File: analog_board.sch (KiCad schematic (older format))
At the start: 48 parts, among them J301 SAMTEC-TSW-105-07-X-D, J302 SAMTEC-TSW-105-07-X-D, J304 SAMTEC-TSW-105-07-X-D, J305 SAMTEC-TSW-105-07-X-D, U1 LM324, U3 AD620, U4 AD620

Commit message: Most wiring is done, no ground yet
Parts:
- added R10, R21: 0R, Resistor_SMD:R_1206_3216Metric_Pad1.42x1.75mm_HandSolder, symbol Device:R
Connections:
- net Current_ch1_out: now also R21.1; no longer C12.1, R6.1
- net Current_sensor_1: now also R10.2; no longer R1.2, R2.2, R3.2, R5.2
- new net: R1.2, R10.1, R2.2, R3.2, R5.2
- new net: C12.1, R21.2, R6.1
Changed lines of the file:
@@
 	1    0    0    -1
 $EndComp
-Text Label 1450 4800 0    50   ~ 0
+Text Label 850  4800 0    50   ~ 0
 Current_sensor_1
 $Comp
@@
 	5250 6100 5250 6350
 Wire Wire Line
-	6300 4600 5700 4600
-Text Label 6300 4600 0    50   ~ 0
+	6900 4600 6300 4600
+Text Label 6900 4600 0    50   ~ 0
 Current_ch1_out
 Wire Wire Line
@@
 Wire Wire Line
 	2150 4750 2150 4800
-Connection ~ 2150 4800
 Wire Wire Line
 	2400 4750 2400 4800
@@
 Wire Wire Line
 	2400 4800 2150 4800
-Wire Wire Line
-	1400 4800 2150 4800
 $Comp
 L Amplifier_Instrumentation:AD620 U4
@@
 NoConn ~ 1550 13250
 NoConn ~ 1550 13350
-Connection ~ 5700 4600
 Wire Wire Line
 	17500 4600 16900 4600
@@
 Wire Wire Line
 	15850 4900 15850 5100
+$Comp
+L Device:R R10
+U 1 1 5C792D0B
+P 1850 4800
+F 0 "R10" V 1643 4800 50  0000 C CNN
+F 1 "0R" V 1734 4800 50  0000 C CNN
+F 2 "Resistor_SMD:R_1206_3216Metric_Pad1.42x1.75mm_HandSolder" V 1780 4800 50  0001 C CNN
+F 3 "~" H 1850 4800 50  0001 C CNN
+	1    1850 4800
+	0    1    1    0
+$EndComp
+Wire Wire Line
+	800  4800 1700 4800
+Wire Wire Line
+	2000 4800 2150 4800
+Connection ~ 2150 4800
+$Comp
+L Device:R R21
+U 1 1 5C7A1976
+P 6150 4600
+F 0 "R21" V 5943 4600 50  0000 C CNN
+F 1 "0R" V 6034 4600 50  0000 C CNN
+F 2 "Resistor_SMD:R_1206_3216Metric_Pad1.42x1.75mm_HandSolder" V 6080 4600 50  0001 C CNN
+F 3 "~" H 6150 4600 50  0001 C CNN
+	1    6150 4600
+	0    1    1    0
+$EndComp
+Wire Wire Line
+	5700 4600 6000 4600
+Connection ~ 5700 4600
 $EndSCHEMATC

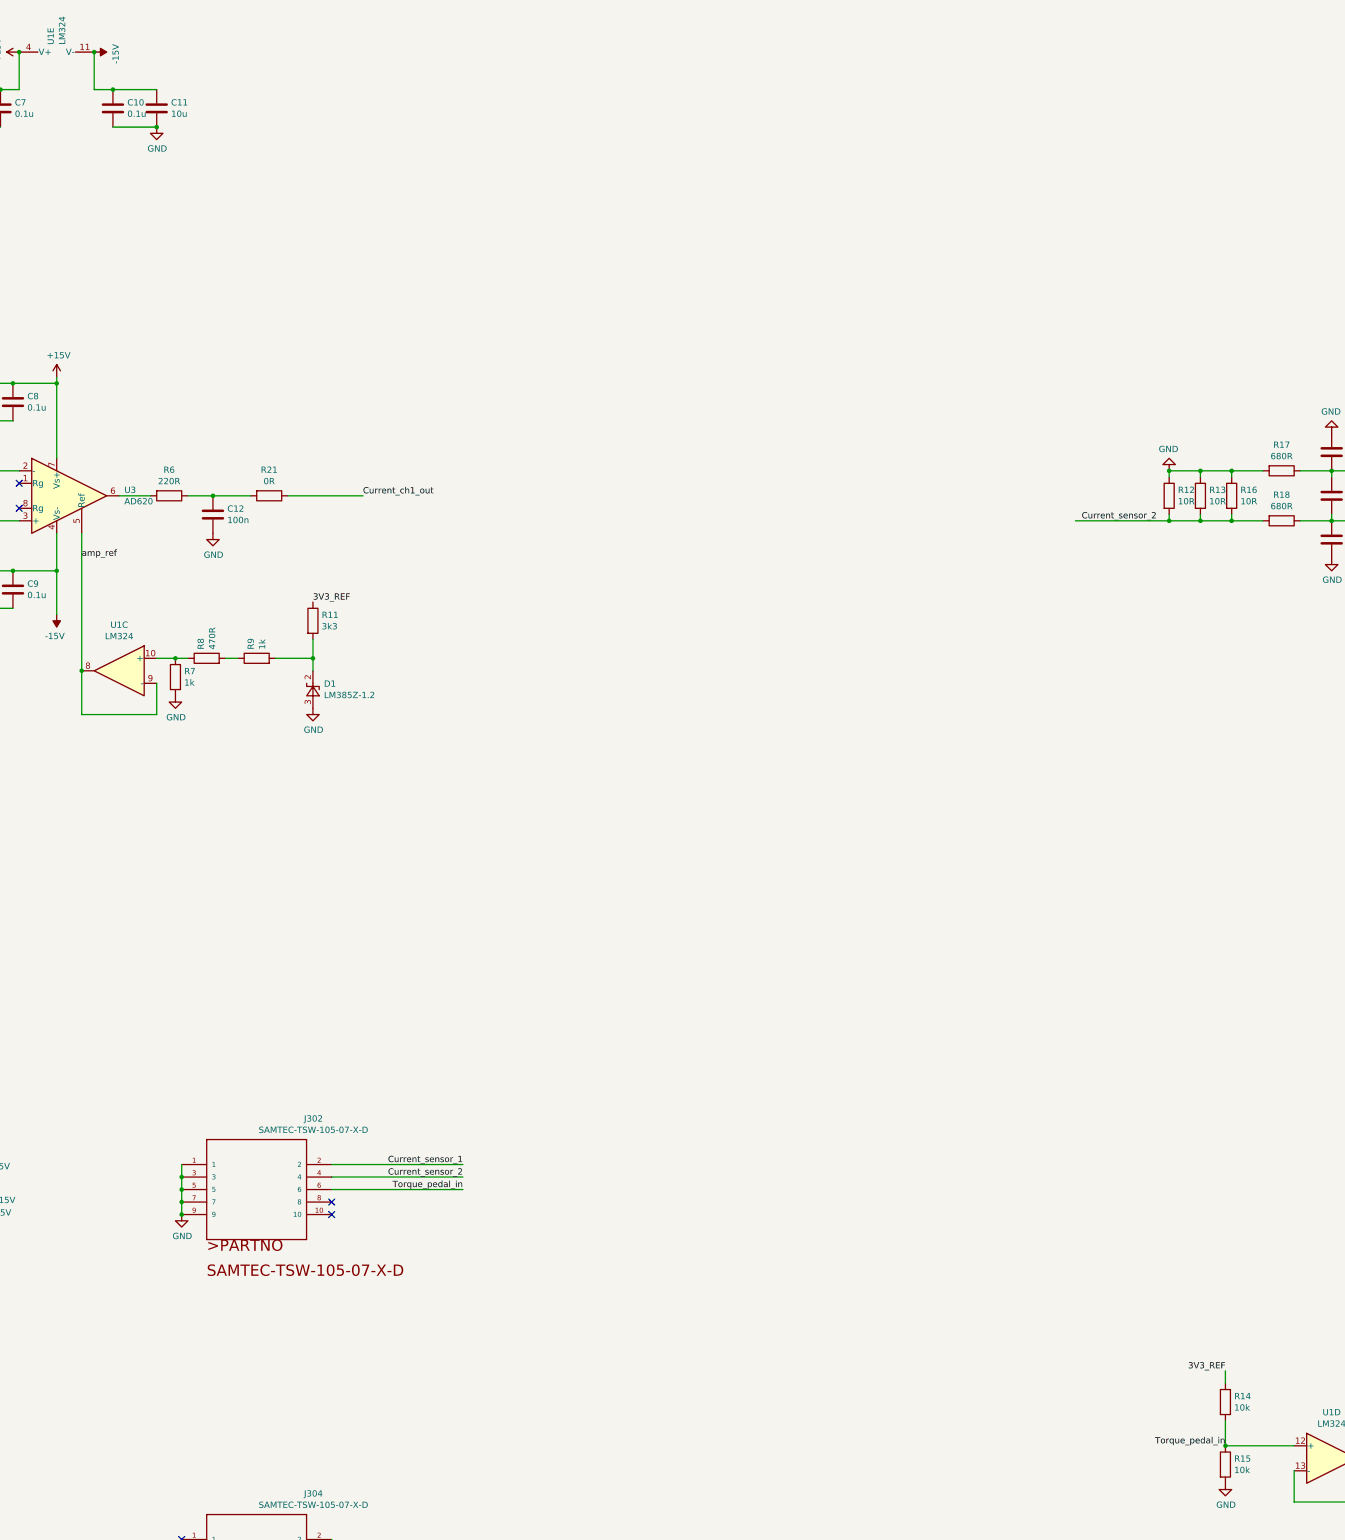
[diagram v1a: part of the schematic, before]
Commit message: All wiring done, except for grounding
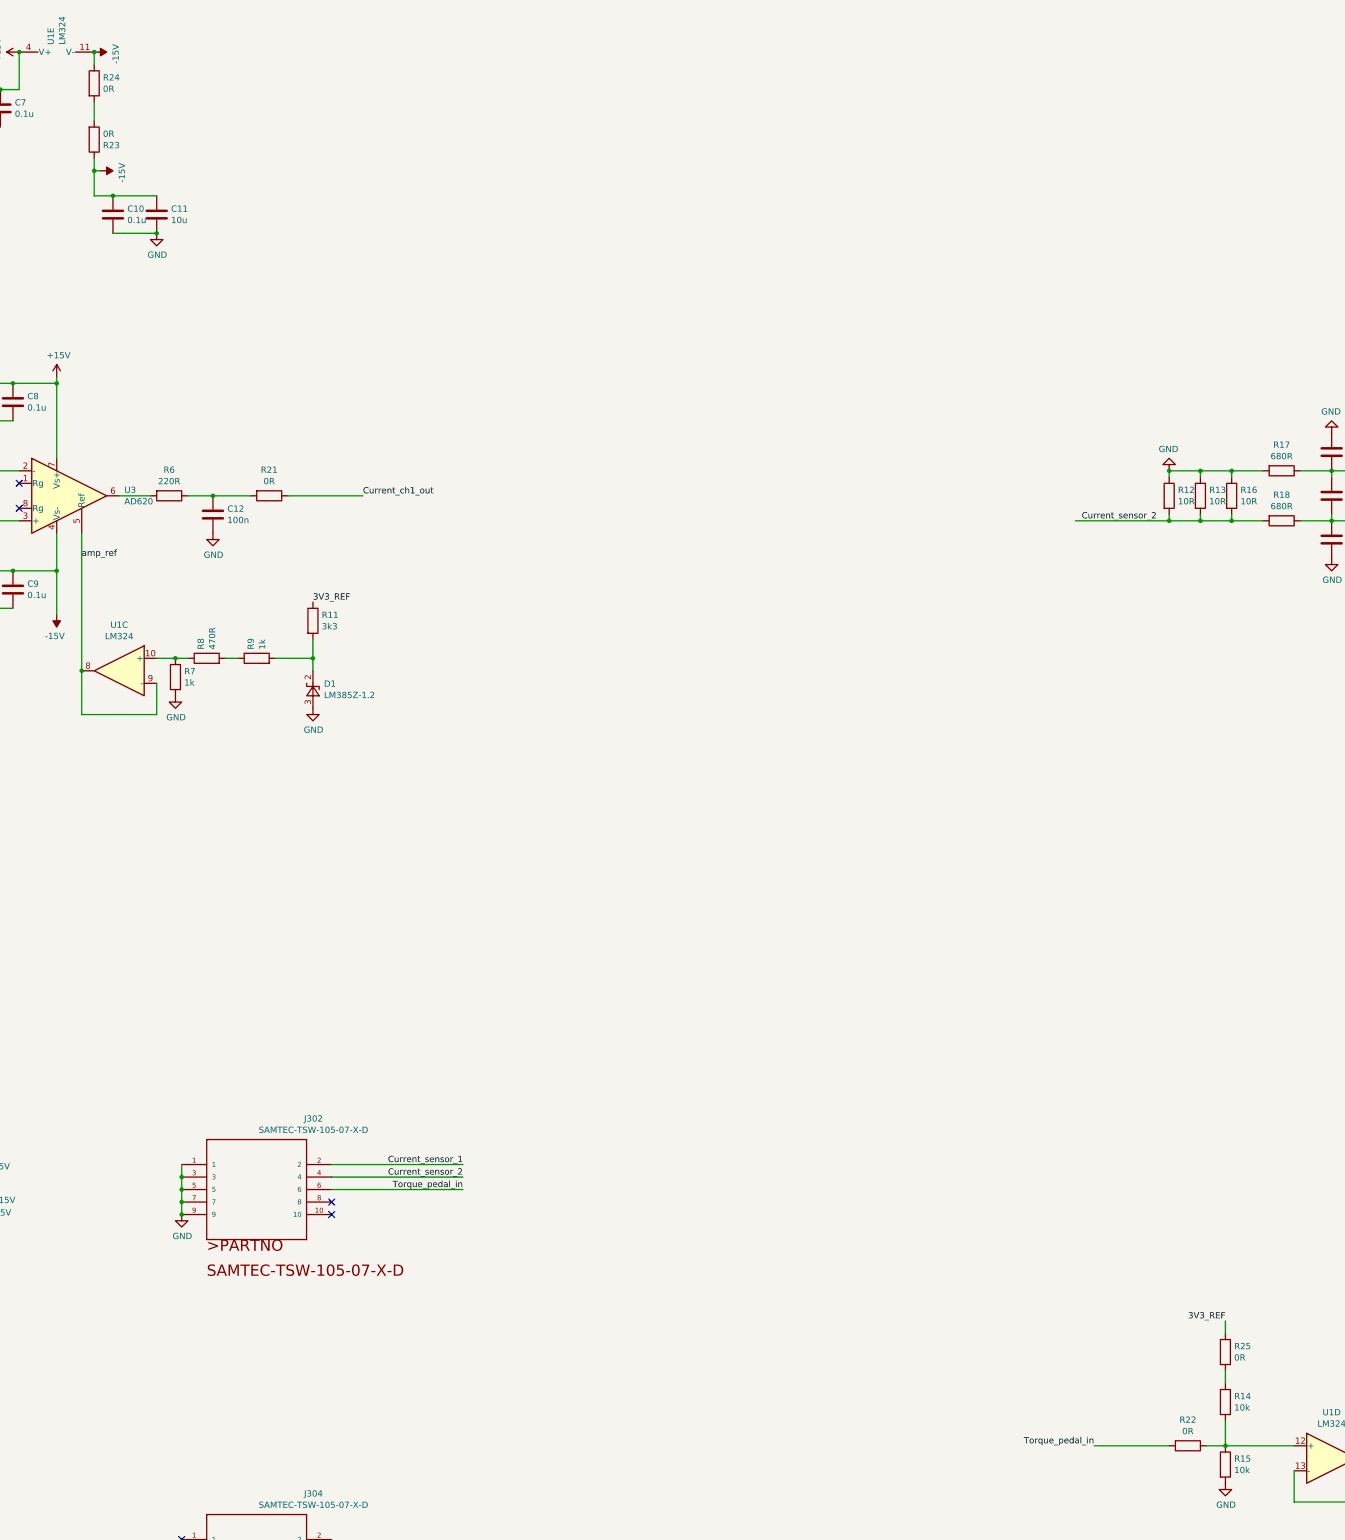
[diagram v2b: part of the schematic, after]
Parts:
- added R22, R24, R25: 0R, Resistor_SMD:R_1206_3216Metric_Pad1.42x1.75mm_HandSolder, symbol Device:R
- added R23: 0R, Resistor_SMD:R_0805_2012Metric_Pad1.15x1.40mm_HandSolder, symbol Device:R
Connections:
- net -15V: now also R23.1, R24.1
- net 3V3_REF: now also R25.1; no longer R14.1
- net Torque_pedal_in: now also R22.2; no longer R14.2, R15.1, U1.12 (+)
- new net: R14.2, R15.1, R22.1, U1.12 (+)
- new net: R14.1, R25.2
- new net: R23.2, R24.2
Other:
- moved on the sheet: C10, C11
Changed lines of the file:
@@
 L Device:C C11
 U 1 1 5C74975A
-P 5250 1500
-F 0 "C11" H 5365 1546 50  0000 L CNN
-F 1 "10u" H 5365 1455 50  0000 L CNN
-F 2 "Capacitor_SMD:C_0805_2012Metric_Pad1.15x1.40mm_HandSolder" H 5288 1350 50  0001 C CNN
-F 3 "~" H 5250 1500 50  0001 C CNN
-	1    5250 1500
+P 5250 2350
+F 0 "C11" H 5365 2396 50  0000 L CNN
+F 1 "10u" H 5365 2305 50  0000 L CNN
+F 2 "Capacitor_SMD:C_0805_2012Metric_Pad1.15x1.40mm_HandSolder" H 5288 2200 50  0001 C CNN
+F 3 "~" H 5250 2350 50  0001 C CNN
+	1    5250 2350
 	1    0    0    -1
 $EndComp
@@
 L power:GND #PWR0116
 U 1 1 5C749765
-P 5250 1650
-F 0 "#PWR0116" H 5250 1400 50  0001 C CNN
-F 1 "GND" H 5255 1477 50  0000 C CNN
-F 2 "" H 5250 1650 50  0001 C CNN
-F 3 "" H 5250 1650 50  0001 C CNN
-	1    5250 1650
+P 5250 2500
+F 0 "#PWR0116" H 5250 2250 50  0001 C CNN
+F 1 "GND" H 5255 2327 50  0000 C CNN
+F 2 "" H 5250 2500 50  0001 C CNN
+F 3 "" H 5250 2500 50  0001 C CNN
+	1    5250 2500
 	1    0    0    -1
 $EndComp
@@
 L Device:C C10
 U 1 1 5C7542C0
-P 4900 1500
-F 0 "C10" H 5015 1546 50  0000 L CNN
-F 1 "0.1u" H 5015 1455 50  0000 L CNN
-F 2 "Capacitor_SMD:C_0805_2012Metric_Pad1.15x1.40mm_HandSolder" H 4938 1350 50  0001 C CNN
-F 3 "~" H 4900 1500 50  0001 C CNN
-	1    4900 1500
-	1    0    0    -1
-$EndComp
-Wire Wire Line
-	4900 1350 5250 1350
-Wire Wire Line
-	4900 1650 5250 1650
-Connection ~ 5250 1650
+P 4900 2350
+F 0 "C10" H 5015 2396 50  0000 L CNN
+F 1 "0.1u" H 5015 2305 50  0000 L CNN
+F 2 "Capacitor_SMD:C_0805_2012Metric_Pad1.15x1.40mm_HandSolder" H 4938 2200 50  0001 C CNN
+F 3 "~" H 4900 2350 50  0001 C CNN
+	1    4900 2350
+	1    0    0    -1
+$EndComp
+Wire Wire Line
+	4900 2200 5250 2200
+Wire Wire Line
+	4900 2500 5250 2500
+Connection ~ 5250 2500
 Wire Wire Line
 	4000 1350 4150 1350
@@
 Connection ~ 4150 1050
 Wire Wire Line
-	4900 1350 4750 1350
-Wire Wire Line
-	4750 1350 4750 1050
-Connection ~ 4900 1350
-Connection ~ 4750 1050
+	4900 2200 4750 2200
+Wire Wire Line
+	4750 2200 4750 2000
+Connection ~ 4900 2200
 $Comp
 L power:+5V #PWR0117
@@
 	1    0    0    -1
 $EndComp
-Text Label 13800 11600 2    50   ~ 0
+Text Label 13800 11200 2    50   ~ 0
 3V3_REF
-Wire Wire Line
-	13800 11700 13800 11600
-Text Label 13800 12200 2    50   ~ 0
+Text Label 12750 12200 2    50   ~ 0
 Torque_pedal_in
 Wire Wire Line
@@
 	5700 4600 6000 4600
 Connection ~ 5700 4600
+$Comp
+L Device:R R22
+U 1 1 5C7B8DFC
+P 13500 12200
+F 0 "R22" V 13293 12200 50  0000 C CNN
+F 1 "0R" V 13384 12200 50  0000 C CNN
+F 2 "Resistor_SMD:R_1206_3216Metric_Pad1.42x1.75mm_HandSolder" V 13430 12200 50  0001 C CNN
+F 3 "~" H 13500 12200 50  0001 C CNN
+	1    13500 12200
+	0    1    1    0
+$EndComp
+Wire Wire Line
+	13800 12200 13650 12200
+Wire Wire Line
+	13350 12200 12750 12200
+$Comp
+L Device:R R23
+U 1 1 5C7D3DFD
+P 4750 1750
+F 0 "R23" H 4820 1796 50  0000 L CNN
+F 1 "0R" H 4820 1705 50  0000 L CNN
+F 2 "Resistor_SMD:R_0805_2012Metric_Pad1.15x1.40mm_HandSolder" V 4680 1750 50  0001 C CNN
+F 3 "~" H 4750 1750 50  0001 C CNN
+	1    4750 1750
+	1    0    0    1
+$EndComp
+$Comp
+L power:-15V #PWR0128
+U 1 1 5C7F0418
+P 4800 2000
+F 0 "#PWR0128" H 4800 2100 50  0001 C CNN
+F 1 "-15V" H 4815 2173 50  0000 C CNN
+F 2 "" H 4800 2000 50  0001 C CNN
+F 3 "" H 4800 2000 50  0001 C CNN
+	1    4800 2000
+	0    1    1    0
+$EndComp
+Wire Wire Line
+	4800 2000 4750 2000
+Connection ~ 4750 2000
+Wire Wire Line
+	4750 2000 4750 1900
+$Comp
+L Device:R R24
+U 1 1 5C80067D
+P 4750 1300
+F 0 "R24" H 4820 1346 50  0000 L CNN
+F 1 "0R" H 4820 1255 50  0000 L CNN
+F 2 "Resistor_SMD:R_1206_3216Metric_Pad1.42x1.75mm_HandSolder" V 4680 1300 50  0001 C CNN
+F 3 "~" H 4750 1300 50  0001 C CNN
+	1    4750 1300
+	1    0    0    -1
+$EndComp
+Wire Wire Line
+	4750 1150 4750 1050
+Connection ~ 4750 1050
+Wire Wire Line
+	4750 1450 4750 1600
+$Comp
+L Device:R R25
+U 1 1 5C7CD4AE
+P 13800 11450
+F 0 "R25" H 13870 11496 50  0000 L CNN
+F 1 "0R" H 13870 11405 50  0000 L CNN
+F 2 "Resistor_SMD:R_1206_3216Metric_Pad1.42x1.75mm_HandSolder" V 13730 11450 50  0001 C CNN
+F 3 "~" H 13800 11450 50  0001 C CNN
+	1    13800 11450
+	1    0    0    -1
+$EndComp
+Wire Wire Line
+	13800 11700 13800 11600
+Wire Wire Line
+	13800 11300 13800 11200
 $EndSCHEMATC

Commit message: All wiring done, awaiting review
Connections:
- net -15V: now also R23.2, R24.2
- net 3V3_REF: now also R14.1, R25.2
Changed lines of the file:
@@
 	1550 10050 1550 10150
 Connection ~ 1550 10050
-Wire Wire Line
-	1550 10150 1550 10250
 Connection ~ 1550 10150
-Wire Wire Line
-	1550 10250 1550 10350
-Connection ~ 1550 10250
 $Comp
 L power:GND #PWR0105
@@
 	1    0    0    -1
 $EndComp
-Connection ~ 1550 10350
 $Comp
 L power:GND #PWR0106
@@
 Connection ~ 4750 1050
 Wire Wire Line
-	4750 1450 4750 1600
+	4750 1450 4750 1500
 $Comp
 L Device:R R25
@@
 Wire Wire Line
 	13800 11300 13800 11200
+Wire Wire Line
+	1550 10150 1550 10250
+Wire Wire Line
+	1550 10250 1550 10350
+Connection ~ 1550 10250
+Connection ~ 1550 10350
+Text Label 13800 11700 2    50   ~ 0
+3V3_REF
+$Comp
+L power:-15V #PWR?
+U 1 1 5C7C6022
+P 4750 1500
+F 0 "#PWR?" H 4750 1600 50  0001 C CNN
+F 1 "-15V" H 4765 1673 50  0000 C CNN
+F 2 "" H 4750 1500 50  0001 C CNN
+F 3 "" H 4750 1500 50  0001 C CNN
+	1    4750 1500
+	0    1    1    0
+$EndComp
+Connection ~ 4750 1500
+Wire Wire Line
+	4750 1500 4750 1600
 $EndSCHEMATC
